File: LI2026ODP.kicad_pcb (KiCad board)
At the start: 2 copper layers, 4 parts, among them J1 9-1437539-2, U1 LM2936MPX-3.0_NOPB, U2 STM32G0B1KET6, U3 max6921aui

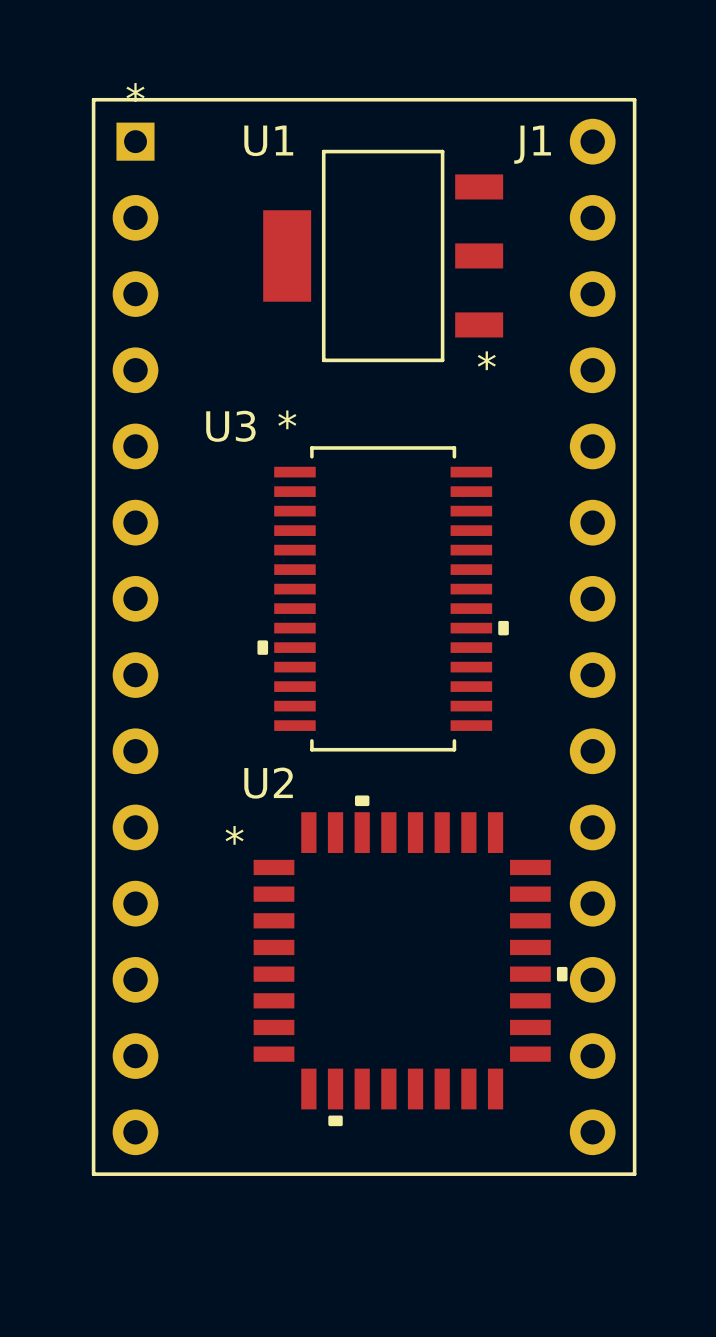
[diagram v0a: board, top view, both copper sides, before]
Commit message: All parts connected.
Waiting for the routing.
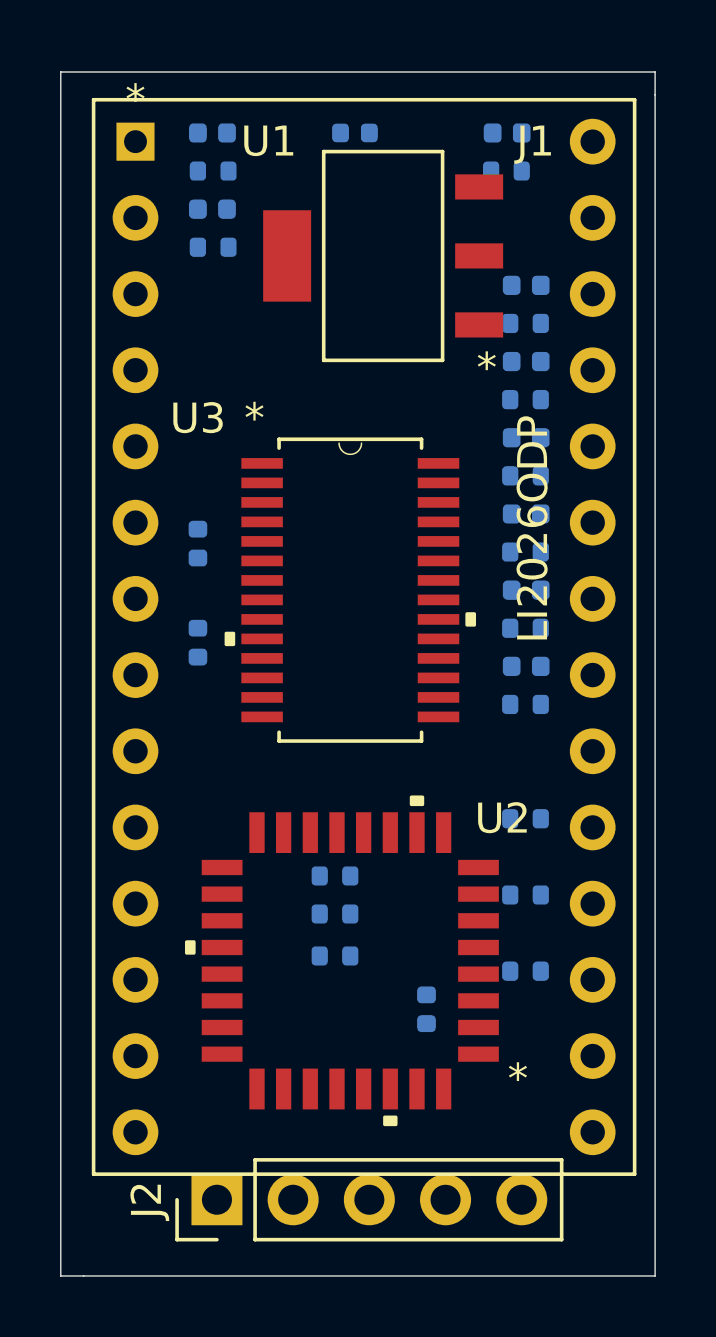
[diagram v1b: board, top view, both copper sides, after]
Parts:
- added C1: C, Capacitor_SMD:C_0402_1005Metric, B.Cu at (124.6, 86.4)
- added C2: C, Capacitor_SMD:C_0402_1005Metric, B.Cu at (119.4, 103.3)
- added C3: C, Capacitor_SMD:C_0402_1005Metric, B.Cu at (119.4, 100.0)
- added C4: C, Capacitor_SMD:C_0402_1005Metric, B.Cu at (127.0, 115.6)
- added D1: D, Diode_SMD:D_0402_1005Metric, B.Cu at (119.9, 86.4)
- added D2: D, Diode_SMD:D_0402_1005Metric, B.Cu at (119.9, 88.9)
- added D3: D, Diode_SMD:D_0402_1005Metric, B.Cu at (130.3, 104.1)
- added D4: D, Diode_SMD:D_0402_1005Metric, B.Cu at (130.3, 101.6)
- added D5: D, Diode_SMD:D_0402_1005Metric, B.Cu at (130.3, 99.1)
- added D6: D, Diode_SMD:D_0402_1005Metric, B.Cu at (130.3, 96.5)
- added D7: D, Diode_SMD:D_0402_1005Metric, B.Cu at (130.3, 94.0)
- added D8: D, Diode_SMD:D_0402_1005Metric, B.Cu at (130.3, 91.4)
- added D9: D, Diode_SMD:D_0402_1005Metric, B.Cu at (129.7, 86.4)
- added J2: Conn_01x05_Male, Connector_PinHeader_2.54mm:PinHeader_1x05_P2.54mm_Vertical, F.Cu at (120.0, 121.9)
- added R1: R, Resistor_SMD:R_0402_1005Metric, B.Cu at (119.9, 90.2)
- added R10: R, Resistor_SMD:R_0402_1005Metric, B.Cu at (130.3, 109.2)
- added R11: R, Resistor_SMD:R_0402_1005Metric, B.Cu at (124.0, 111.1)
- added R12: R, Resistor_SMD:R_0402_1005Metric, B.Cu at (130.3, 111.8)
- added R13: R, Resistor_SMD:R_0402_1005Metric, B.Cu at (124.0, 112.4)
- added R14: R, Resistor_SMD:R_0402_1005Metric, B.Cu at (130.3, 114.3)
- added R15: R, Resistor_SMD:R_0402_1005Metric, B.Cu at (124.0, 113.8)
- added R2: R, Resistor_SMD:R_0402_1005Metric, B.Cu at (119.9, 87.6)
- added R3: R, Resistor_SMD:R_0402_1005Metric, B.Cu at (129.7, 87.6)
- added R4: R, Resistor_SMD:R_0402_1005Metric, B.Cu at (130.3, 92.7)
- added R5: R, Resistor_SMD:R_0402_1005Metric, B.Cu at (130.3, 95.2)
- added R6: R, Resistor_SMD:R_0402_1005Metric, B.Cu at (130.3, 97.8)
- added R7: R, Resistor_SMD:R_0402_1005Metric, B.Cu at (130.3, 100.3)
- added R8: R, Resistor_SMD:R_0402_1005Metric, B.Cu at (130.3, 102.9)
- added R9: R, Resistor_SMD:R_0402_1005Metric, B.Cu at (130.3, 105.4)
- moved U2 1.73 mm to (124.5, 114.0), turned to 180 degrees
- moved U3 1.13 mm to (124.5, 101.6)
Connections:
- J1 pad 10: Net-(J1-Pad10) -> /SEG_E
- J1 pad 11: Net-(J1-Pad11) -> /SEG_C
- J1 pad 12: Net-(J1-Pad12) -> /SEG_D
- J1 pad 13: Net-(J1-Pad13) -> /SEG_DP
- J1 pad 14: Net-(J1-Pad14) -> /+25V
- J1 pad 17: Net-(J1-Pad17) -> /KEY1
- J1 pad 18: Net-(J1-Pad18) -> /KEY2
- J1 pad 19: Net-(J1-Pad19) -> /KEY3
- J1 pad 4: Net-(J1-Pad4) -> GND
- J1 pad 6: Net-(J1-Pad6) -> /SEG_A
- J1 pad 7: Net-(J1-Pad7) -> /SEG_F
- J1 pad 8: Net-(J1-Pad8) -> /SEG_B
- J1 pad 9: Net-(J1-Pad9) -> /SEG_G
- U1 pad 1: Net-(U1-Pad1) -> /+25V
- U1 pad 2: Net-(U1-Pad2) -> GND
- U1 pad 3: Net-(U1-Pad3) -> +3V3
- U1 pad 4: Net-(U1-Pad4) -> GND
- U2 pad 10: Net-(U2-Pad10) -> /RKEY2
- U2 pad 11: Net-(U2-Pad11) -> /RKEY3
- U2 pad 12: Net-(U2-Pad12) -> /SCK
- U2 pad 13: Net-(U2-Pad13) -> /LOAD
- U2 pad 14: Net-(U2-Pad14) -> /MOSI
- U2 pad 24: Net-(U2-Pad24) -> /SWCLK
- U2 pad 25: Net-(U2-Pad25) -> /SWDIO
- U2 pad 30: Net-(U2-Pad30) -> /LPUART2_TX
- U2 pad 4: Net-(U2-Pad4) -> +3V3
- U2 pad 5: Net-(U2-Pad5) -> GND
- U2 pad 6: Net-(U2-Pad6) -> /NRST
- U2 pad 9: Net-(U2-Pad9) -> /RKEY1
- U3 pad 1: Net-(U3-Pad1) -> /D1
- U3 pad 10: Net-(U3-Pad10) -> /SEG_G
- U3 pad 11: Net-(U3-Pad11) -> /SEG_E
- U3 pad 12: Net-(U3-Pad12) -> /SEG_C
- U3 pad 13: Net-(U3-Pad13) -> /SEG_D
- U3 pad 14: Net-(U3-Pad14) -> /SEG_DP
- U3 pad 18: Net-(U3-Pad18) -> /D8
- U3 pad 19: Net-(U3-Pad19) -> /D7
- U3 pad 2: Net-(U3-Pad2) -> /D0
- U3 pad 20: Net-(U3-Pad20) -> +3V3
- U3 pad 21: Net-(U3-Pad21) -> GND
- U3 pad 22: Net-(U3-Pad22) -> /SCK
- U3 pad 23: Net-(U3-Pad23) -> /LOAD
- U3 pad 24: Net-(U3-Pad24) -> /D6
- U3 pad 25: Net-(U3-Pad25) -> /D5
- U3 pad 26: Net-(U3-Pad26) -> /D4
- U3 pad 27: Net-(U3-Pad27) -> /D3
- U3 pad 28: Net-(U3-Pad28) -> /D2
- U3 pad 3: Net-(U3-Pad3) -> /SEG_A
- U3 pad 4: Net-(U3-Pad4) -> /SEG_F
- U3 pad 5: Net-(U3-Pad5) -> /SEG_B
- U3 pad 6: Net-(U3-Pad6) -> /MOSI
- U3 pad 7: Net-(U3-Pad7) -> +3V3
- U3 pad 8: Net-(U3-Pad8) -> /+25V
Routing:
- added copper zone on In1.Cu, net GND
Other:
- board outline added: 19.8 x 40.1 mm
- copper layers 2 -> 4
- board text added: "LI2026ODP"

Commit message: Change SMD from 1005M to 1608M
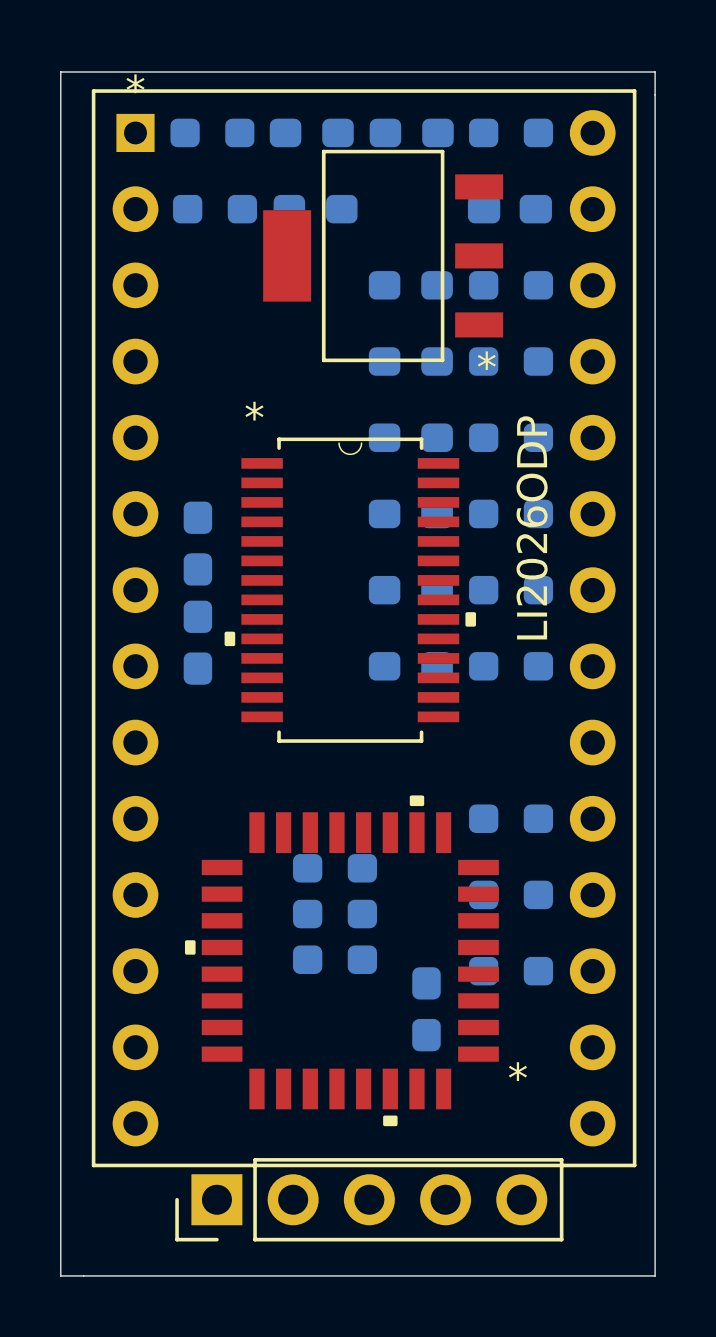
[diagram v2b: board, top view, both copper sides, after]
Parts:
- C1, C2, C3, C4: footprint Capacitor_SMD:C_0402_1005Metric -> Capacitor_SMD:C_0603_1608Metric_Pad1.08x0.95mm_HandSolder
- D1, D2, D3, D4, D5, D6, D7, D8, D9: footprint Diode_SMD:D_0402_1005Metric -> Diode_SMD:D_0603_1608Metric_Pad1.05x0.95mm_HandSolder
- R1, R10, R11, R12, R13, R14, R15, R2, R3, R4, R5, R6, R7, R8, R9: footprint Resistor_SMD:R_0402_1005Metric -> Resistor_SMD:R_0603_1608Metric_Pad0.98x0.95mm_HandSolder
- moved C1 5.76 mm to (129.8, 88.9)
- moved D3 3.85 mm to (126.5, 104.1)
- moved D4 3.85 mm to (126.5, 101.6)
- moved D5 3.85 mm to (126.5, 99.1)
- moved D6 3.85 mm to (126.5, 96.5)
- moved D7 3.85 mm to (126.5, 94.0)
- moved D8 3.85 mm to (126.5, 91.4)
- moved D2 3.44 mm to (123.3, 88.9)
- moved D1 3.31 mm to (123.2, 86.4)
- moved D9 3.18 mm to (126.5, 86.4)
- moved R6 1.36 mm to (129.8, 96.5), turned to 0 degrees
- moved R8 1.36 mm to (129.8, 101.6), turned to 0 degrees
- moved R4 1.36 mm to (129.8, 91.4), turned to 0 degrees
- moved R5 1.36 mm to (129.8, 94.0), turned to 0 degrees
- moved R7 1.36 mm to (129.8, 99.1), turned to 0 degrees
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
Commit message: layout finished.
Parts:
- moved C3 4.28 mm to (123.4, 98.7)
- moved C2 4.16 mm to (123.4, 104.2)
- moved C4 2.03 mm to (127.0, 113.5), turned to 90 degrees
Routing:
- net +3V3: track 0.00 -> 47.8 mm, vias 0 -> 5
- net /+25V: track 0.00 -> 37.0 mm, vias 0 -> 2
- net GND: track 0.00 -> 31.5 mm, vias 0 -> 11
- net /D3: track 0.00 -> 16.8 mm, vias 0 -> 2
- net /D2: track 0.00 -> 13.9 mm, vias 0 -> 2
- net /SEG_DP: track 0.00 -> 13.3 mm, vias 0 -> 2
- net /SCK: track 0.00 -> 13.2 mm, vias 0 -> 2
- net /D1: track 0.00 -> 12.8 mm, vias 0 -> 1
- net /RKEY1: track 0.00 -> 12.3 mm, vias 0 -> 1
- net /NRST: track 0.00 -> 11.7 mm, vias 0 -> 1
- net /LOAD: track 0.00 -> 11.6 mm, vias 0 -> 2
- net /MOSI: track 0.00 -> 11.5 mm, vias 0 -> 2
- net /SEG_D: track 0.00 -> 11.4 mm
- net /D0: track 0.00 -> 11.0 mm, vias 0 -> 1
- net /SEG_C: track 0.00 -> 9.70 mm
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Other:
- board size 19.8 x 40.1 mm -> 18.8 x 39.1 mm
- net class Default: trace_width 0.25 -> 0.2; via_dia 0.8 -> 0.6; via_drill 0.4 -> 0.3
- rule via_min_size: 0.4 -> 0.5
- board text added: "GND"
- board text added: "NRST"
- board text added: "SWCLK"
- board text added: "SWDIO"
- board text added: "TX"

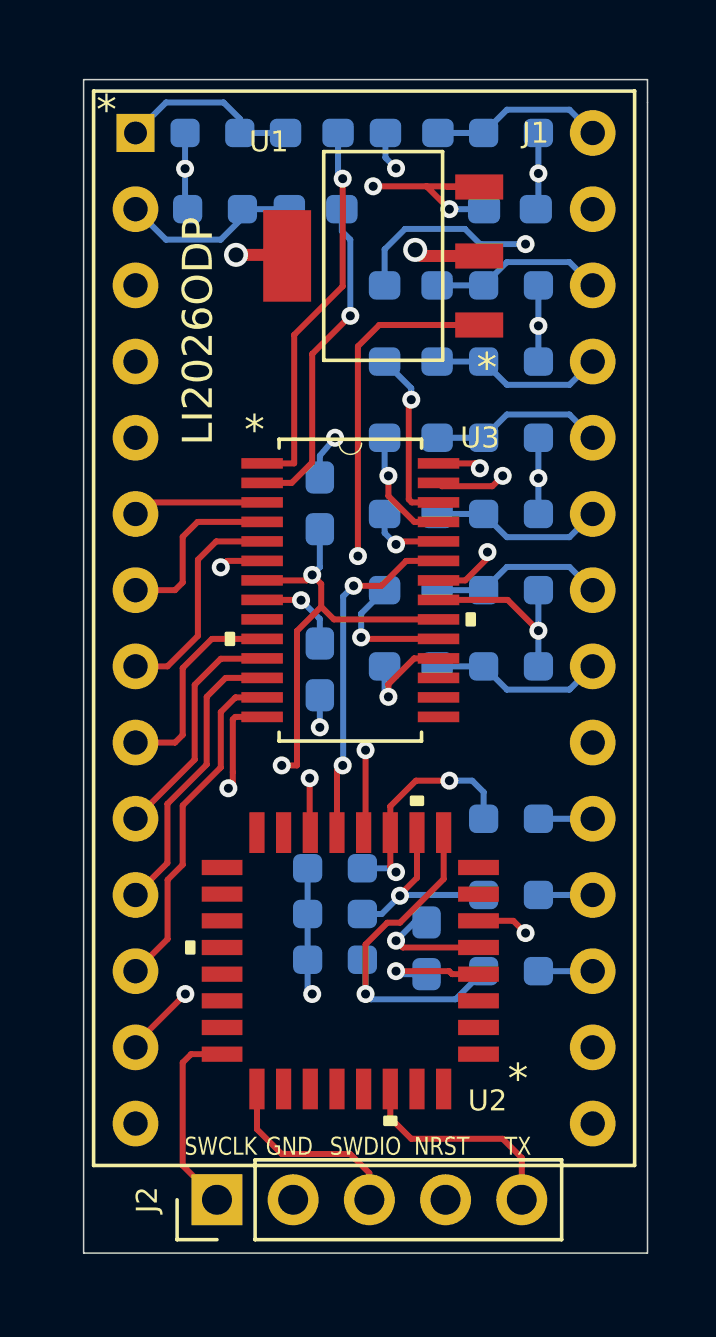
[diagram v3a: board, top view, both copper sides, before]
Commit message: Fix the BLANK bug and change layout
- BLANK was incorrectly tied with 3.3v
- Make layer 3 as +3.3v
- Make 25v line as 0.4mm
- Change RKEY1,2,3 pins for the simple layout.
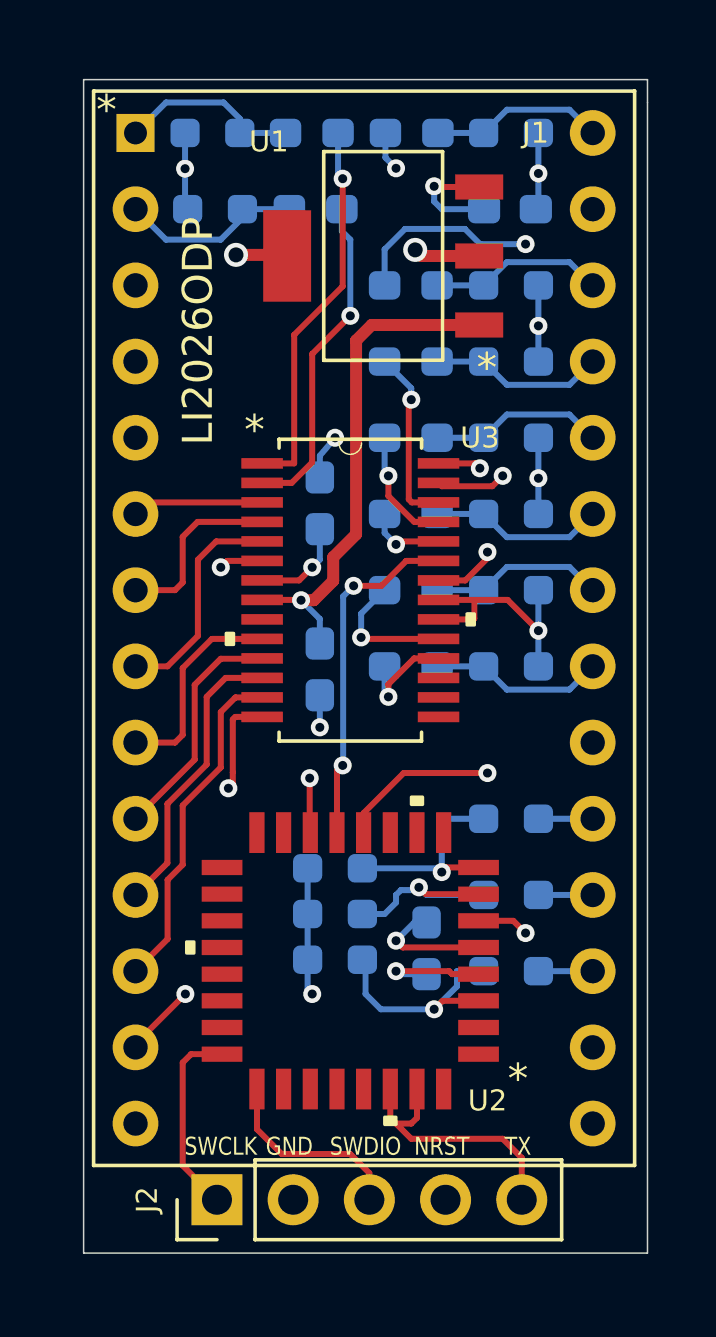
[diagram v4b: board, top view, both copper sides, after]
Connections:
- U2 pad 10: /RKEY2 -> Net-(U2-Pad10)
- U2 pad 11: /RKEY3 -> Net-(U2-Pad11)
- U2 pad 3: Net-(U2-Pad3) -> /RKEY1
- U2 pad 31: Net-(U2-Pad31) -> /LPUART2_TX
- U2 pad 7: Net-(U2-Pad7) -> /RKEY2
- U2 pad 8: Net-(U2-Pad8) -> /RKEY3
- U2 pad 9: /RKEY1 -> Net-(U2-Pad9)
- U3 pad 20: +3V3 -> GND
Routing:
- net +3V3: track 47.8 -> 11.1 mm, vias 5 -> 3
- net /RKEY1: track 12.3 -> 7.60 mm
- net GND: track 31.5 -> 33.3 mm
- net /LPUART2_TX: track 7.29 -> 9.03 mm
- net /SCK: track 13.2 -> 14.9 mm
- net /RKEY3: track 7.96 -> 7.01 mm, vias 2 -> 1
- net /+25V: track 37.0 -> 36.8 mm, vias 2 -> 1
- added copper zone on In2.Cu, net +3V3

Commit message: Change voltage regulator
from 3.0 to 3.3v
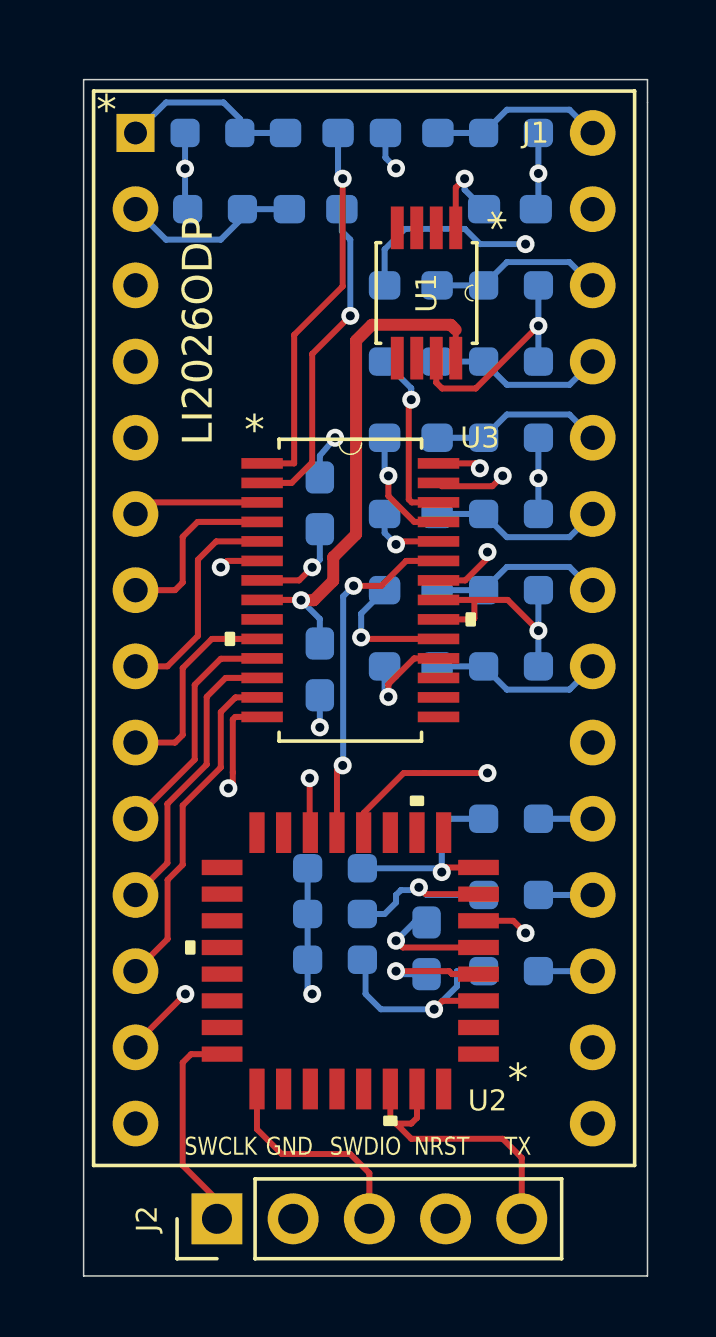
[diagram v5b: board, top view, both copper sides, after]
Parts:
- C1: value C -> 4.7u
- C2, C3, C4: value C -> 0.1u
- J1: value 9-1437539-2 -> CON28-B700X1400_DIP
- R1, R2, R3, R4, R5, R6, R7, R8, R9: value R -> 15k
- R10, R12, R14: value R -> 27k
- R11, R13, R15: value R -> 3.3k
- U1: value LM2936MPX-3.0_NOPB -> MUA08A_TEX; footprint LM2936MXP:LM2936MPX-3.0&slash_NOPB -> LM2936MM:LM2936MM-3.3
- U2: value STM32G0B1KET6 -> LQFP_0B1KET6_STM
- U3: value max6921aui -> 21-0066J_28_MXM
- moved U1 1.90 mm to (127.0, 91.7), turned to 270 degrees
- moved J2 0.64 mm to (120.0, 122.6)
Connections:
- U1 pad 1: /+25V -> +3V3
- U1 pad 2: GND -> Net-(U1-Pad2)
- U1 pad 3: +3V3 -> Net-(U1-Pad3)
- U1 pad 4: GND -> Net-(U1-Pad4)
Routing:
- net GND: track 33.3 -> 34.5 mm, vias 11 -> 9
- net +3V3: track 11.1 -> 10.3 mm
- net /LPUART2_TX: track 9.03 -> 9.67 mm
- net /SWDIO: track 6.58 -> 7.22 mm
- net /SWCLK: track 6.48 -> 7.11 mm
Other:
- board size 18.8 x 39.1 mm -> 18.8 x 39.9 mm
